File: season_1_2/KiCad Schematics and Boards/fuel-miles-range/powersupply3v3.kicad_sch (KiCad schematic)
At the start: 2 parts

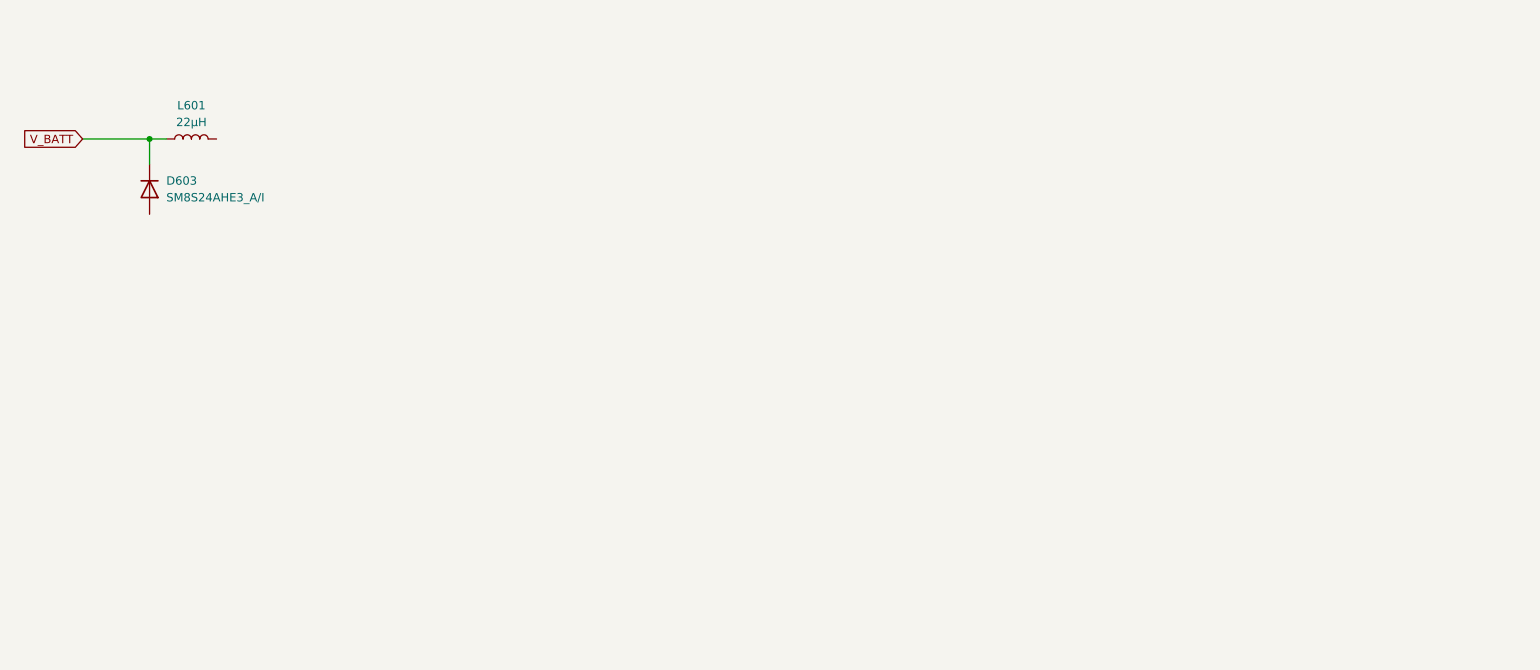
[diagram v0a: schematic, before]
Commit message: Added lots of electronic devices and routes
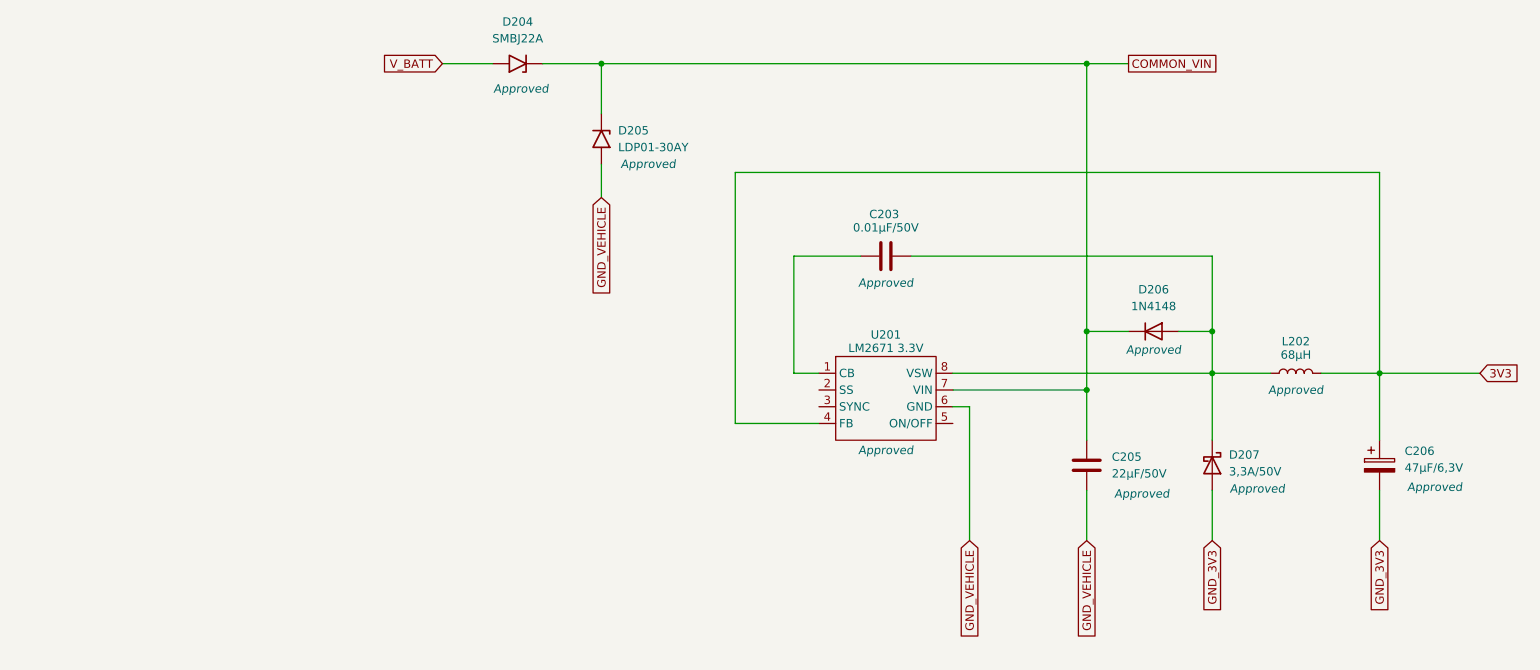
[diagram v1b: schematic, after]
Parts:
- removed D603: SM8S24AHE3_A/I, Diode_SMD:D_SOD-123, symbol Diode:BAV16W
- removed L601: 22µH, symbol Device:L
- added C203: 0.01µF/50V, Capacitor_SMD:C_1206_3216Metric, symbol Device:C
- added C205: 22µF/50V, symbol Device:C
- added C206: 47µF/6,3V, Capacitor_SMD:CP_Elec_10x12.6, symbol Device:C_Polarized
- added D204: SMBJ22A, Diode_SMD:D_SOD-123, symbol Diode:SMF5V0A
- added D205: LDP01-30AY, Package_TO_SOT_SMD:TO-263-2, symbol Diode:1N62xxA
- added D206: 1N4148, Diode_SMD:D_SOD-523, symbol Diode:1N4148WT
- added D207: 3,3A/50V, Diode_SMD:D_SOD-323, symbol Device:D_Schottky
- added L202: 68µH, Inductor_SMD:L_Murata_LQH55DN_5.7x5.0mm, symbol Device:L
- added U201: LM2671 3.3V, Package_SO:SOIC-8_5.3x5.3mm_P1.27mm, symbol Code99_VREG:LM2671
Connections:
- net V_BATT: now also D204.2 (A2)
- new net: C203.1, D206.2 (A), D207.1 (K), L202.1, U201.8 (VSW)
- new net: C203.2, U201.1 (CB)
- new net 3V3: C206.1, L202.2, U201.4 (FB)
- new net COMMON_VIN: C205.1, D204.1 (A1), D205.1 (A1), D206.1 (K), U201.7 (VIN)
- new net GND_3V3: C206.2, D207.2 (A)
- new net GND_VEHICLE: C205.2, D205.2 (A2), U201.6 (GND)
